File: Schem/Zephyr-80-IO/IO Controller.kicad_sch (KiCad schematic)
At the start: 43 parts, among them IC1 Z80CTC, IC2 Z80SIO, IC3 Z80SIO, J5 Conn_01x08_Pin, SW1 SW_Push, SW2 SW_Push, U1 74AHCT125, U15 PIC18F57Q84-I/PT, U2 74AHCT1G125, U4 74AHC595, U5 74AHC595, U6 74HC138

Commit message: Part #s
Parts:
- R36, R37, R38, R4: value 100k -> 10k
- U1: MANUFACTURER_PART_NUMBER (none) -> SN74AHCT125QPWRQ1
- U2: MANUFACTURER_PART_NUMBER (none) -> SN74AHCT1G125DBVR
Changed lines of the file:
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@@
 			)
 		)
+		(property "MANUFACTURER_PART_NUMBER" "SN74AHCT125QPWRQ1"
+			(at 234.95 205.74 0)
+			(hide yes)
+			(show_name no)
+			(do_not_autoplace no)
+			(effects
+				(font
+					(size 1.27 1.27)
+				)
+			)
+		)
 		(pin "4"
 		)
@@
 			)
 		)
+		(property "MANUFACTURER_PART_NUMBER" "SN74AHCT125QPWRQ1"
+			(at 146.05 228.6 0)
+			(hide yes)
+			(show_name no)
+			(do_not_autoplace no)
+			(effects
+				(font
+					(size 1.27 1.27)
+				)
+			)
+		)
 		(pin "4"
 		)
@@
 			)
 		)
+		(property "MANUFACTURER_PART_NUMBER" "SN74AHCT1G125DBVR"
+			(at 160.02 311.15 0)
+			(hide yes)
+			(show_name no)
+			(do_not_autoplace no)
+			(effects
+				(font
+					(size 1.27 1.27)
+				)
+			)
+		)
 		(pin "3"
 		)
@@
 			)
 		)
+		(property "MANUFACTURER_PART_NUMBER" "SN74AHCT125QPWRQ1"
+			(at 226.06 219.71 0)
+			(hide yes)
+			(show_name no)
+			(do_not_autoplace no)
+			(effects
+				(font
+					(size 1.27 1.27)
+				)
+			)
+		)
 		(pin "4"
 		)
@@
 			)
 		)
-		(property "Value" "100k"
+		(property "Value" "10k"
 			(at 61.976 247.65 0)
 			(show_name no)
@@
 			)
 		)
+		(property "MANUFACTURER_PART_NUMBER" "SN74AHCT125QPWRQ1"
+			(at 223.52 185.42 0)
+			(hide yes)
+			(show_name no)
+			(do_not_autoplace no)
+			(effects
+				(font
+					(size 1.27 1.27)
+				)
+			)
+		)
 		(pin "4"
 		)
@@
 			)
 		)
-		(property "Value" "100k"
+		(property "Value" "10k"
 			(at 23.876 247.904 0)
 			(show_name no)
@@
 			)
 		)
+		(property "MANUFACTURER_PART_NUMBER" "SN74AHCT125QPWRQ1"
+			(at 228.6 168.91 0)
+			(hide yes)
+			(show_name no)
+			(do_not_autoplace no)
+			(effects
+				(font
+					(size 1.27 1.27)
+				)
+			)
+		)
 		(pin "4"
 		)
@@
 			)
 		)
-		(property "Value" "100k"
+		(property "Value" "10k"
 			(at 31.75 247.65 0)
 			(show_name no)
@@
 			)
 		)
-		(property "Value" "100k"
+		(property "Value" "10k"
 			(at 39.116 247.65 0)
 			(show_name no)

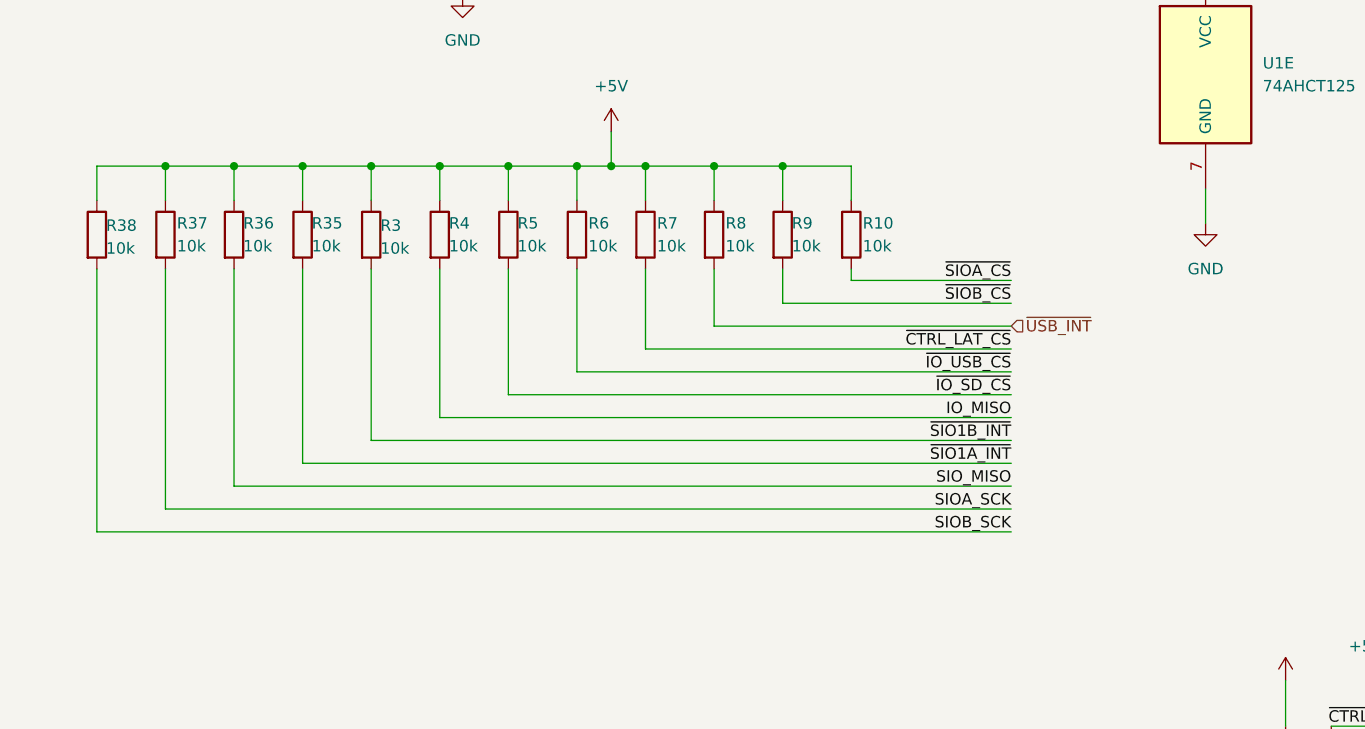
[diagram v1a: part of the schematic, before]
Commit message: updated the pullups for the power on sequence pins
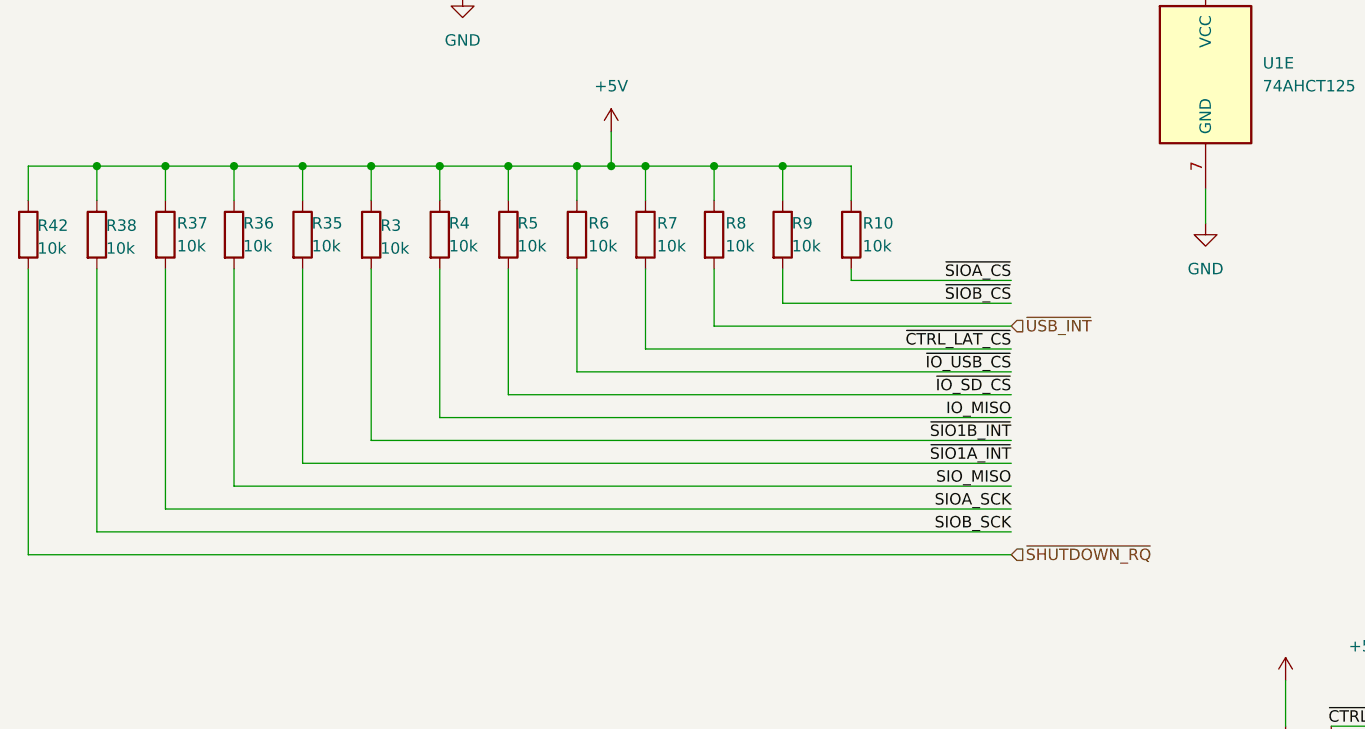
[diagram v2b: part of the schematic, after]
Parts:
- added R42: 10k, Resistor_SMD:R_0603_1608Metric, symbol Device:R
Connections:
- net +5V: now also R42.1
- net ~{SHUTDOWN_RQ}: now also R42.2
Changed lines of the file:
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@@
 	)
 	(junction
+		(at 22.86 238.76)
+		(diameter 0)
+		(color 0 0 0 0)
+	)
+	(junction
 		(at 113.03 100.33)
 		(diameter 0)
@@
 	(wire
 		(pts
+			(xy 15.24 250.19) (xy 15.24 281.94)
+		)
+		(stroke
+			(width 0)
+			(type default)
+		)
+	)
+	(wire
+		(pts
 			(xy 233.68 219.71) (xy 243.84 219.71)
 		)
@@
 	(wire
 		(pts
+			(xy 15.24 281.94) (xy 124.46 281.94)
+		)
+		(stroke
+			(width 0)
+			(type default)
+		)
+	)
+	(wire
+		(pts
 			(xy 302.26 99.06) (xy 316.23 99.06)
 		)
@@
 	(wire
 		(pts
+			(xy 15.24 242.57) (xy 15.24 238.76)
+		)
+		(stroke
+			(width 0)
+			(type default)
+		)
+	)
+	(wire
+		(pts
 			(xy 396.24 88.9) (xy 410.21 88.9)
 		)
@@
 	(wire
 		(pts
+			(xy 15.24 238.76) (xy 22.86 238.76)
+		)
+		(stroke
+			(width 0)
+			(type default)
+		)
+	)
+	(wire
+		(pts
 			(xy 40.64 203.2) (xy 52.07 203.2)
 		)
@@
 		)
 	)
+	(hierarchical_label "~{SHUTDOWN_RQ}"
+		(shape input)
+		(at 124.46 281.94 0)
+		(effects
+			(font
+				(size 1.27 1.27)
+			)
+			(justify left)
+		)
+	)
 	(hierarchical_label "~{WAIT}"
 		(shape passive)
@@
 					(unit 1)
 				)
+			)
+		)
+	)
+	(symbol
+		(lib_id "Device:R")
+		(at 15.24 246.38 0)
+		(unit 1)
+		(body_style 1)
+		(exclude_from_sim no)
+		(in_bom yes)
+		(on_board yes)
+		(in_pos_files yes)
+		(dnp no)
+		(property "Reference" "R42"
+			(at 16.256 245.364 0)
+			(show_name no)
+			(do_not_autoplace no)
+			(effects
+				(font
+					(size 1.27 1.27)
+				)
+				(justify left)
+			)
+		)
+		(property "Value" "10k"
+			(at 16.256 247.904 0)
+			(show_name no)
+			(do_not_autoplace no)
+			(effects
+				(font
+					(size 1.27 1.27)
+				)
+				(justify left)
+			)
+		)
+		(property "Footprint" "Resistor_SMD:R_0603_1608Metric"
+			(at 13.462 246.38 90)
+			(hide yes)
+			(show_name no)
+			(do_not_autoplace no)
+			(effects
+				(font
+					(size 1.27 1.27)
+				)
+			)
+		)
+		(property "Datasheet" ""
+			(at 15.24 246.38 0)
+			(hide yes)
+			(show_name no)
+			(do_not_autoplace no)
+			(effects
+				(font
+					(size 1.27 1.27)
+				)
+			)
+		)
+		(property "Description" "Resistor"
+			(at 15.24 246.38 0)
+			(hide yes)
+			(show_name no)
+			(do_not_autoplace no)
+			(effects
+				(font
+					(size 1.27 1.27)
+				)
+			)
+		)
+		(property "KLC_S4.2_3V3OUT" ""
+			(at 15.24 246.38 0)
+			(hide yes)
+			(show_name no)
+			(do_not_autoplace no)
+			(effects
+				(font
+					(size 1.27 1.27)
+				)
+			)
+		)
+		(property "KLC_S4.2_VCC" ""
+			(at 15.24 246.38 0)
+			(hide yes)
+			(show_name no)
+			(do_not_autoplace no)
+			(effects
+				(font
+					(size 1.27 1.27)
+				)
+			)
+		)
+		(property "MANUFACTURER_PART_NUMBER" "RC0603FR-0710KL"
+			(at 15.24 246.38 0)
+			(hide yes)
+			(show_name no)
+			(do_not_autoplace no)
+			(effects
+				(font
+					(size 1.27 1.27)
+				)
+			)
+		)
+		(pin "1"
+		)
+		(pin "2"
+		)
+		(instances
+			(project "Zephyr-80-IO"
+				(path "/db33a8e4-587d-4e74-8d3f-b68910957121/40aeb9cf-7834-4efc-b850-38b27b4487fe"
+					(reference "R42")
+					(unit 1)
+				)

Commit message: Corrections post review
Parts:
- R4: now not fitted
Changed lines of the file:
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@@
 		(on_board yes)
 		(in_pos_files yes)
-		(dnp no)
+		(dnp yes)
 		(property "Reference" "R4"
 			(at 61.976 245.11 0)
